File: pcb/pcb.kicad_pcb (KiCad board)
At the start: 2 copper layers, 49 x 31 mm, 37 parts, among them J1 Conn_02x08_Odd_Even, J2 B2B-PH-K-S_LF__SN_, J3 USB_C_Receptacle, J4 Conn_01x04, Q1 MMUN2211LT1G, SW1 SW_SPST, U1 TPS61090, U2 MCP73871-1AA

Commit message: fixed some mistakes
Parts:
- S1: footprint Button_Switch_THT:SW_CuK_JS202011AQN_DPDT_Angled -> Button_Switch_SMD:SW_DPDT_CK_JS202011JCQN
- moved S1 3.76 mm to (162.0, 71.4)
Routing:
- net Net-(R5-Pad2): track 23.1 -> 30.6 mm, vias 1 -> 2
- net GND: track 256.0 -> 259.9 mm

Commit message: revd to v1.1
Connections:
- U1 pad 17: Net-(U1-Pad17) -> GND
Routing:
- net GND: track 259.9 -> 93.7 mm, vias 15 -> 8
- net VBAT: track 87.1 -> 56.6 mm, vias 5 -> 4
- net Net-(C6-Pad1): track 51.4 -> 35.9 mm
- net Net-(L1-Pad2): track 18.2 -> 27.7 mm, vias 0 -> 2
- net Net-(R5-Pad2): track 30.6 -> 23.0 mm, vias 2 -> 0
- net Net-(Q1-Pad2): track 8.83 -> 2.15 mm, vias 2 -> 0
- net PI_BCM_23: track 57.4 -> 61.5 mm, vias 1 -> 2
- net 5.0V: track 73.7 -> 77.1 mm
- net Net-(D1-Pad2): track 44.3 -> 46.4 mm
- net PI_BCM_18_PWM0: track 24.9 -> 23.0 mm
- net PI_BCM_3_SCL: track 26.4 -> 24.5 mm
- net PI_BCM_2_SDA: track 20.6 -> 22.5 mm
- net Net-(D3-Pad2): track 12.9 -> 11.3 mm
- net Net-(J3-PadA5): track 14.6 -> 13.8 mm
- net VBUS: track 61.2 -> 61.9 mm, vias 5 -> 6
- added copper zone on B.Cu, net GND
- added copper zone on F.Cu, net GND
- removed copper zone on B.Cu, net Net-(U1-Pad2)
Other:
- board text added: "5V"
- board text added: "GND"
- board text added: "SCL"
- board text added: "SDA"

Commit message: cleaned up a few traces
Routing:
- net GND: track 93.7 -> 68.9 mm, vias 8 -> 2
- net PI_BCM_23: track 61.5 -> 59.9 mm

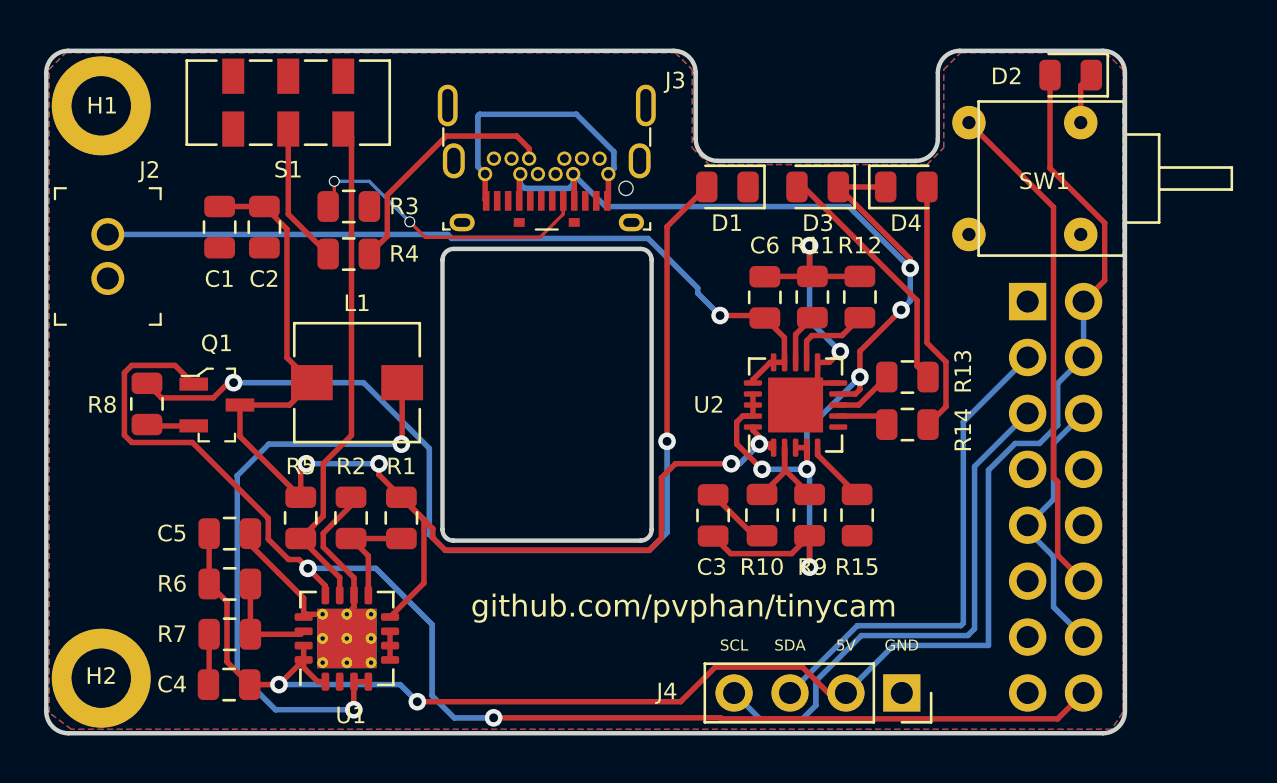
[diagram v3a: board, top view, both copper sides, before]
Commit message: increased track widths for power
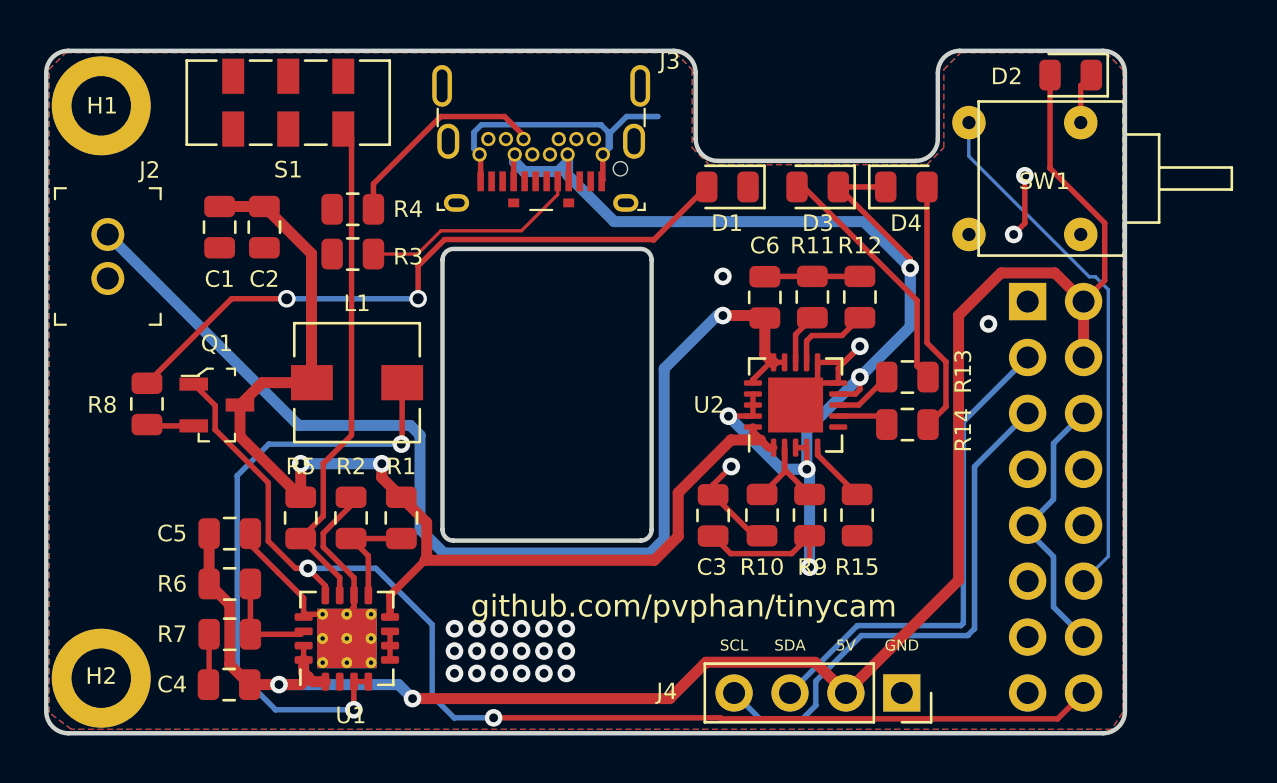
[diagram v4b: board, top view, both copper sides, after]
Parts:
- moved R3 2.17 mm to (164.9, 78.2), turned to 0 degrees
- moved R4 2.04 mm to (164.9, 76.2)
- moved J3 0.92 mm to (173.5, 74.9)
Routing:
- net Net-(D1-Pad2): track 46.4 -> 30.0 mm
- net Net-(C6-Pad1): track 35.9 -> 51.5 mm
- net PI_BCM_23: track 59.9 -> 52.8 mm
- net GND: track 68.9 -> 64.6 mm, vias 2 -> 24
- net Net-(J3-PadA5): track 13.8 -> 10.1 mm, vias 2 -> 0
- net 5.0V: track 77.1 -> 80.6 mm
- net VBAT: track 56.6 -> 53.8 mm, vias 4 -> 2
- net Net-(J3-PadB5): track 11.3 -> 9.76 mm
- net VBUS: track 61.9 -> 63.2 mm, vias 6 -> 5
- net PI_BCM_18_PWM0: track 23.0 -> 24.1 mm
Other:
- rule trace_min: 0.2 -> 0.15
